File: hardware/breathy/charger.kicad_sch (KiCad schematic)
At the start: 35 parts, among them Q1 MMBT3906, Q2 2SAR572D3TL1, Q5 MMBT3906, Q8 PMV37ENEAR, SW1 SW_Push, U1 AZ431AN, U4 TLV9002, U6 TLV9002, U7 AZ431AN

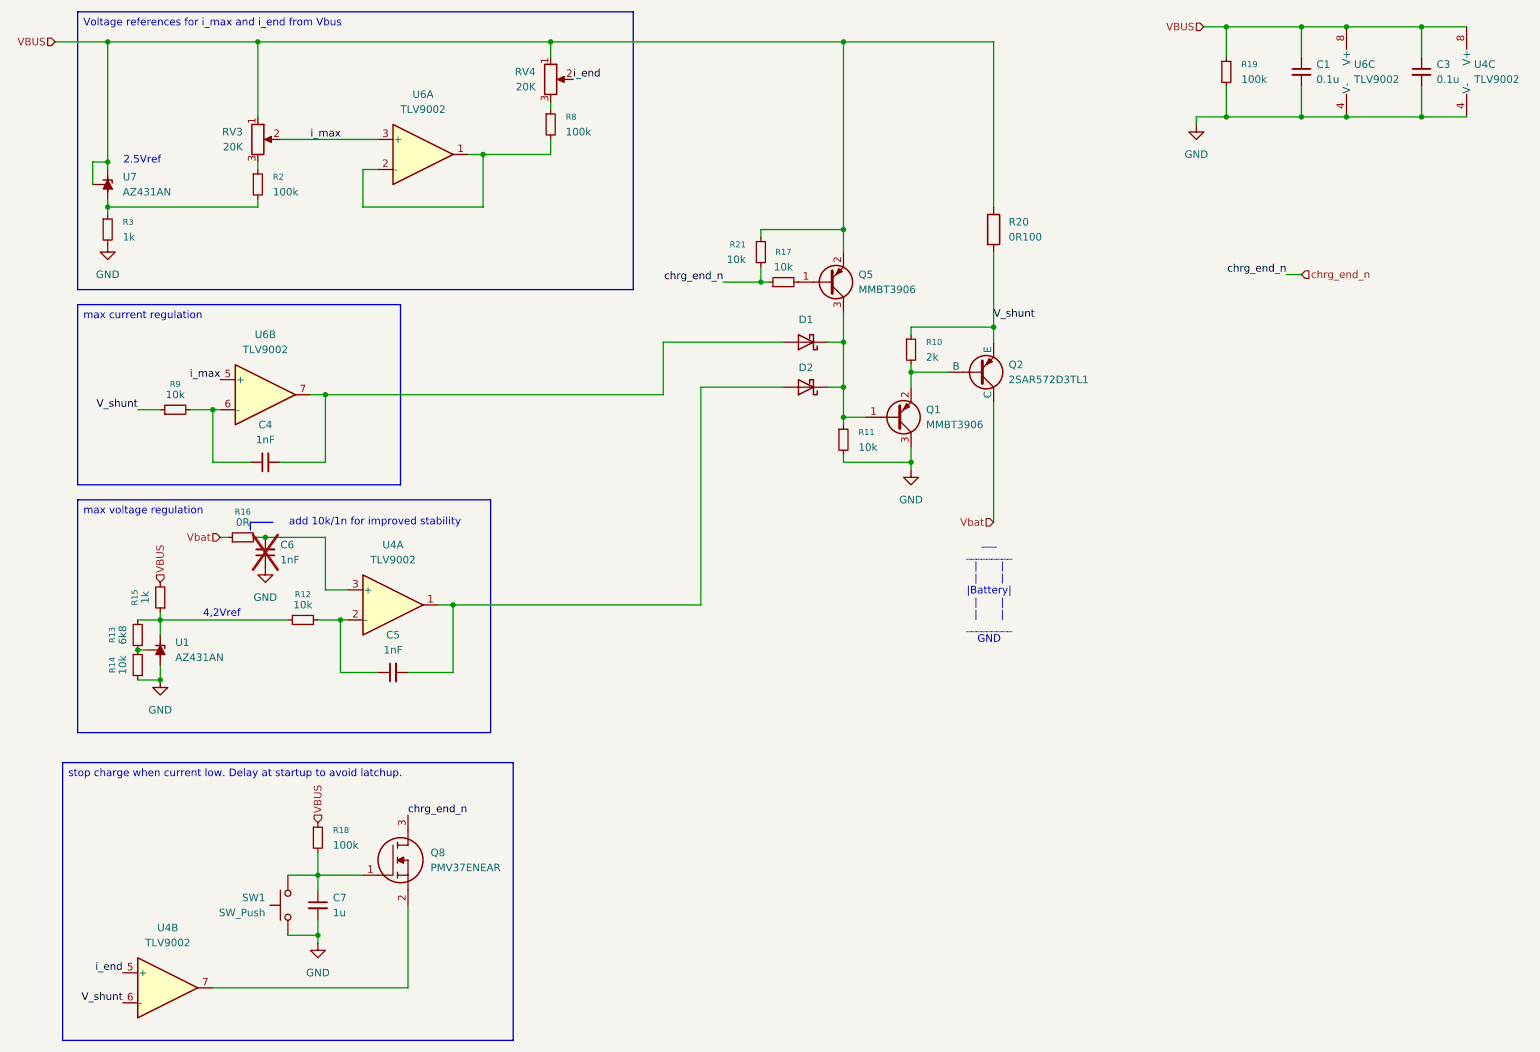
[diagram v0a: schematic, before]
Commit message: test points, headers, indicators, no battery sim
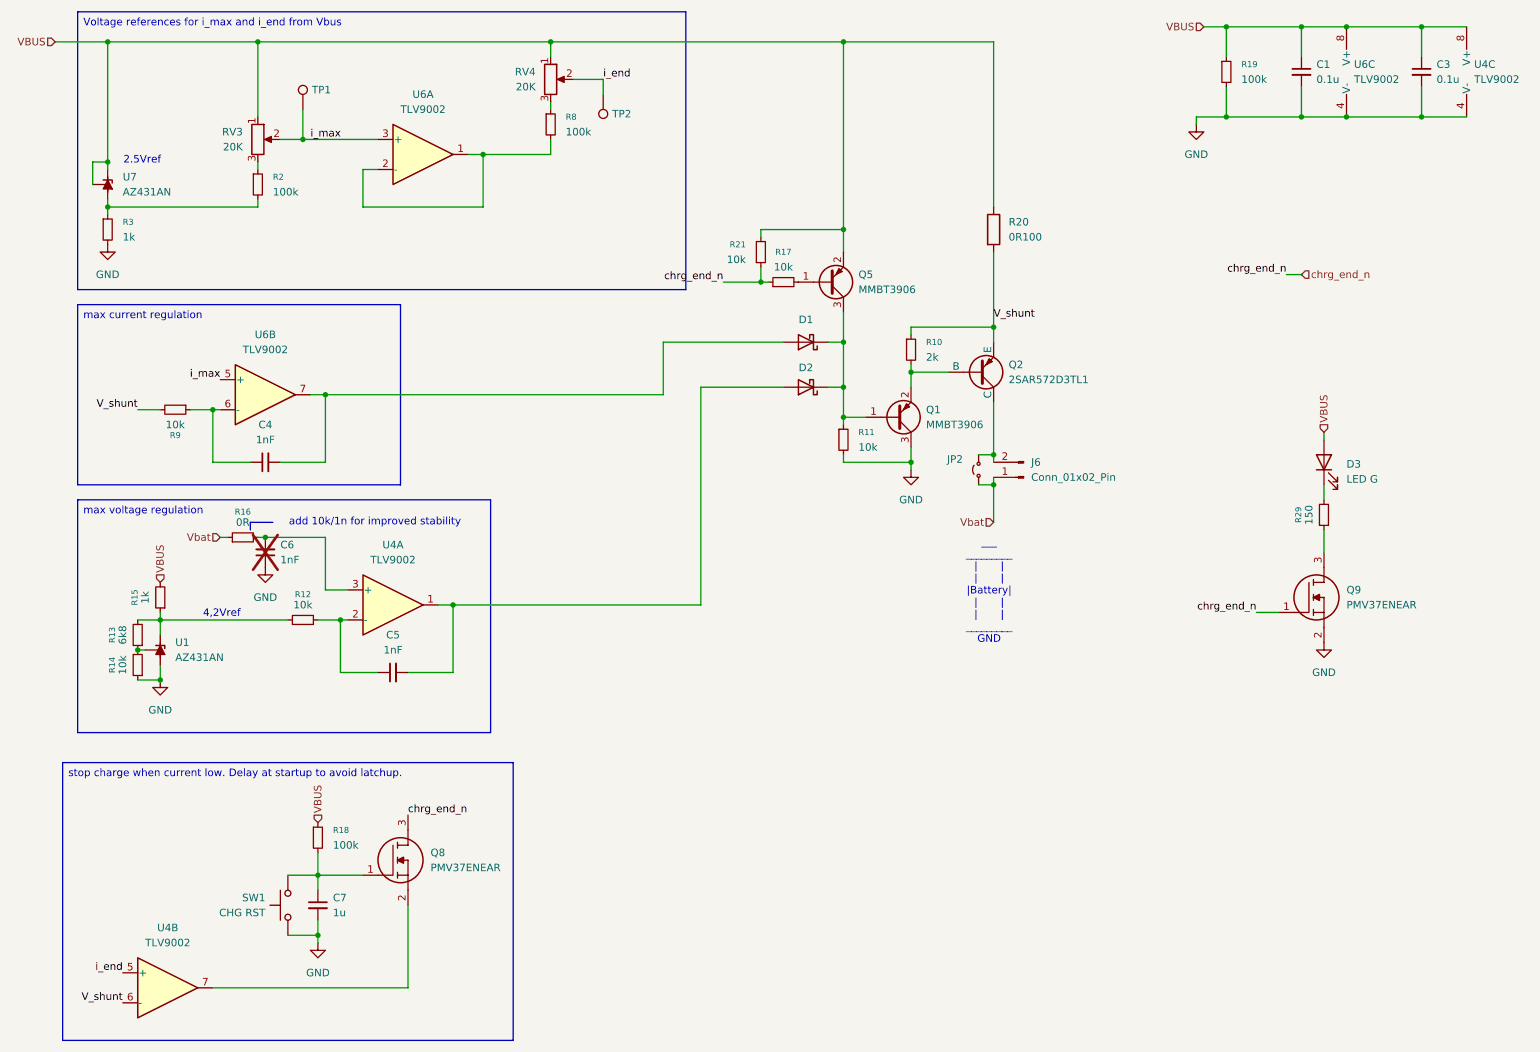
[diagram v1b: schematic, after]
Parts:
- added D3: LED G, LED_SMD:LED_1206_3216Metric, symbol Device:LED
- added J6: Conn_01x02_Pin, symbol Connector:Conn_01x02_Pin
- added JP2: Jumper_2_Small_Open, Jumper:SolderJumper-2_P1.3mm_Open_TrianglePad1.0x1.5mm, symbol Jumper:Jumper_2_Small_Open
- added Q9: PMV37ENEAR, PMV37ENEAR:SOT95P230X110-3N, symbol PMV37ENEAR:PMV37ENEAR
- added R29: 150, Resistor_SMD:R_1206_3216Metric_Pad1.30x1.75mm_HandSolder, symbol Device:R_Small
- added TP1: (no value), symbol Connector:TestPoint
- added TP2: TestPoint, symbol Connector:TestPoint
- SW1: value SW_Push -> CHG RST
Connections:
- net GND: now also Q9.2
- net VBUS: now also D3.2 (A)
- net V_shunt: now also R9.2; no longer R9.1
- net Vbat: now also J6.1 (Pin_1), JP2.1 (A); no longer Q2.2 (C)
- net chrg_end_n: now also Q9.1
- net i_end: now also TP2.1
- net i_max: now also TP1.1
- net at C4.1, U6.6 (-): now also R9.1; no longer R9.2
- new net: J6.2 (Pin_2), JP2.2 (B), Q2.2 (C)
- new net: D3.1 (K), R29.2
- new net: Q9.3, R29.1
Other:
- moved on the sheet: R9

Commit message: adding pdf schematics
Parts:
- C10: renamed from C4; footprint (none) -> Capacitor_SMD:C_0805_2012Metric
- C11: renamed from C6; footprint (none) -> Capacitor_SMD:C_0805_2012Metric
- C12: renamed from C5; footprint (none) -> Capacitor_SMD:C_0805_2012Metric
- C13: renamed from C7; footprint (none) -> Capacitor_SMD:C_1206_3216Metric
- C8: renamed from C1; footprint (none) -> Capacitor_SMD:C_0805_2012Metric
- C9: renamed from C3; footprint (none) -> Capacitor_SMD:C_0805_2012Metric
- J5: renamed from J6; footprint (none) -> Connector_PinHeader_2.54mm:PinHeader_1x02_P2.54mm_Vertical
- R12: renamed from R19; footprint (none) -> Resistor_SMD:R_1206_3216Metric
- R13: renamed from R8; footprint (none) -> Resistor_SMD:R_1206_3216Metric
- R14: renamed from R2; footprint (none) -> Resistor_SMD:R_1206_3216Metric
- R15: renamed from R3; footprint (none) -> Resistor_SMD:R_1206_3216Metric
- R17: renamed from R21; footprint Resistor_SMD:R_1206_3216Metric_Pad1.30x1.75mm_HandSolder -> Resistor_SMD:R_0805_2012Metric
- R18: renamed from R17; footprint Resistor_SMD:R_1206_3216Metric_Pad1.30x1.75mm_HandSolder -> Resistor_SMD:R_0805_2012Metric
- R19: renamed from R10; value 2k -> 5.1k; footprint (none) -> Resistor_SMD:R_0805_2012Metric
- R20: renamed from R9; footprint Resistor_SMD:R_1206_3216Metric_Pad1.30x1.75mm_HandSolder -> Resistor_SMD:R_0805_2012Metric
- R21: renamed from R11; footprint Resistor_SMD:R_1206_3216Metric_Pad1.30x1.75mm_HandSolder -> Resistor_SMD:R_0805_2012Metric
- R22: renamed from R29; footprint Resistor_SMD:R_1206_3216Metric_Pad1.30x1.75mm_HandSolder -> Resistor_SMD:R_0805_2012Metric
- R23: renamed from R16; footprint Resistor_SMD:R_1206_3216Metric_Pad1.30x1.75mm_HandSolder -> Resistor_SMD:R_0805_2012Metric
- R24: renamed from R15; footprint Resistor_SMD:R_1206_3216Metric_Pad1.30x1.75mm_HandSolder -> Resistor_SMD:R_1206_3216Metric
- R25: renamed from R12; footprint Resistor_SMD:R_1206_3216Metric_Pad1.30x1.75mm_HandSolder -> Resistor_SMD:R_0805_2012Metric
- R26: renamed from R13; footprint Resistor_SMD:R_1206_3216Metric_Pad1.30x1.75mm_HandSolder -> Resistor_SMD:R_0805_2012Metric
- R27: renamed from R14; footprint Resistor_SMD:R_1206_3216Metric_Pad1.30x1.75mm_HandSolder -> Resistor_SMD:R_0805_2012Metric
- R28: renamed from R18; footprint (none) -> Resistor_SMD:R_1206_3216Metric
- TP3: renamed from TP2; footprint (none) -> TestPoint:TestPoint_Pad_D1.5mm
- TP4: renamed from TP1; value (none) -> TestPoint; footprint (none) -> TestPoint:TestPoint_Pad_D1.5mm
- renumbered D1 to D2, D2 to D3, D3 to D4, Q5 to Q2, Q2 to Q3, Q1 to Q4, Q9 to Q5, Q8 to Q6, R20 to R16, RV4 to RV1, RV3 to RV2, SW1 to SW3, U6 to U5, U4 to U6, U1 to U8
